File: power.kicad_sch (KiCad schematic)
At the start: 18 parts

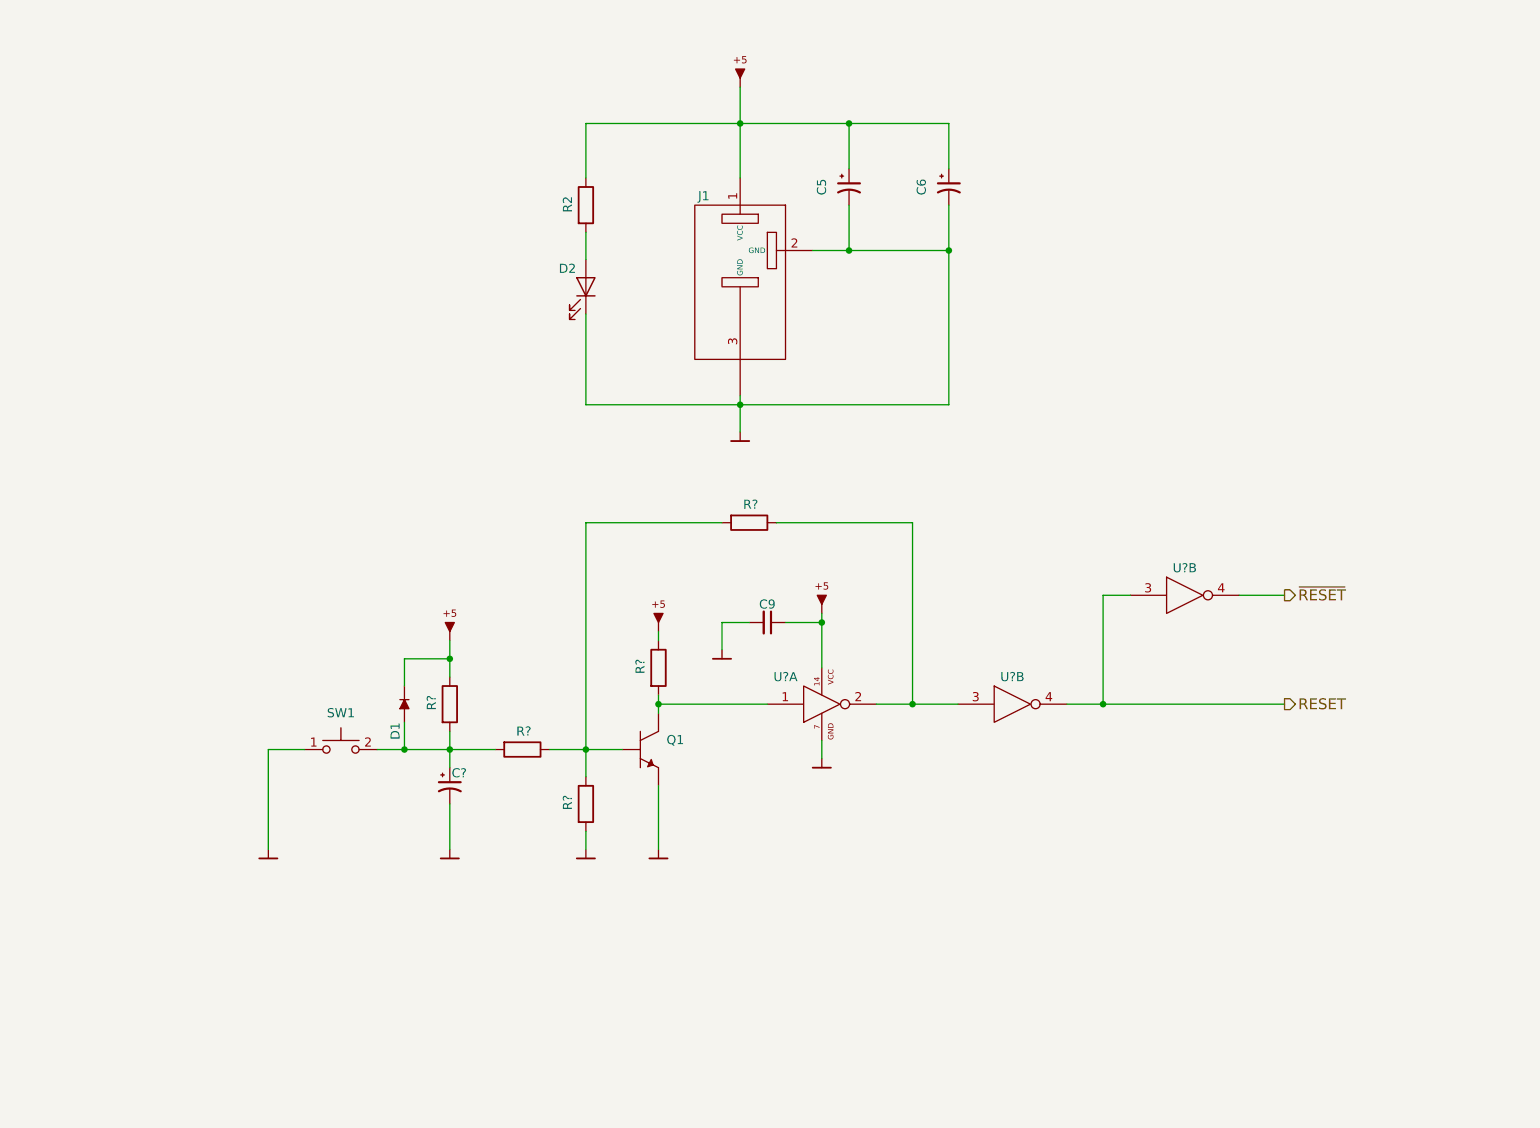
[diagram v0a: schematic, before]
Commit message: Implement power transform circuit
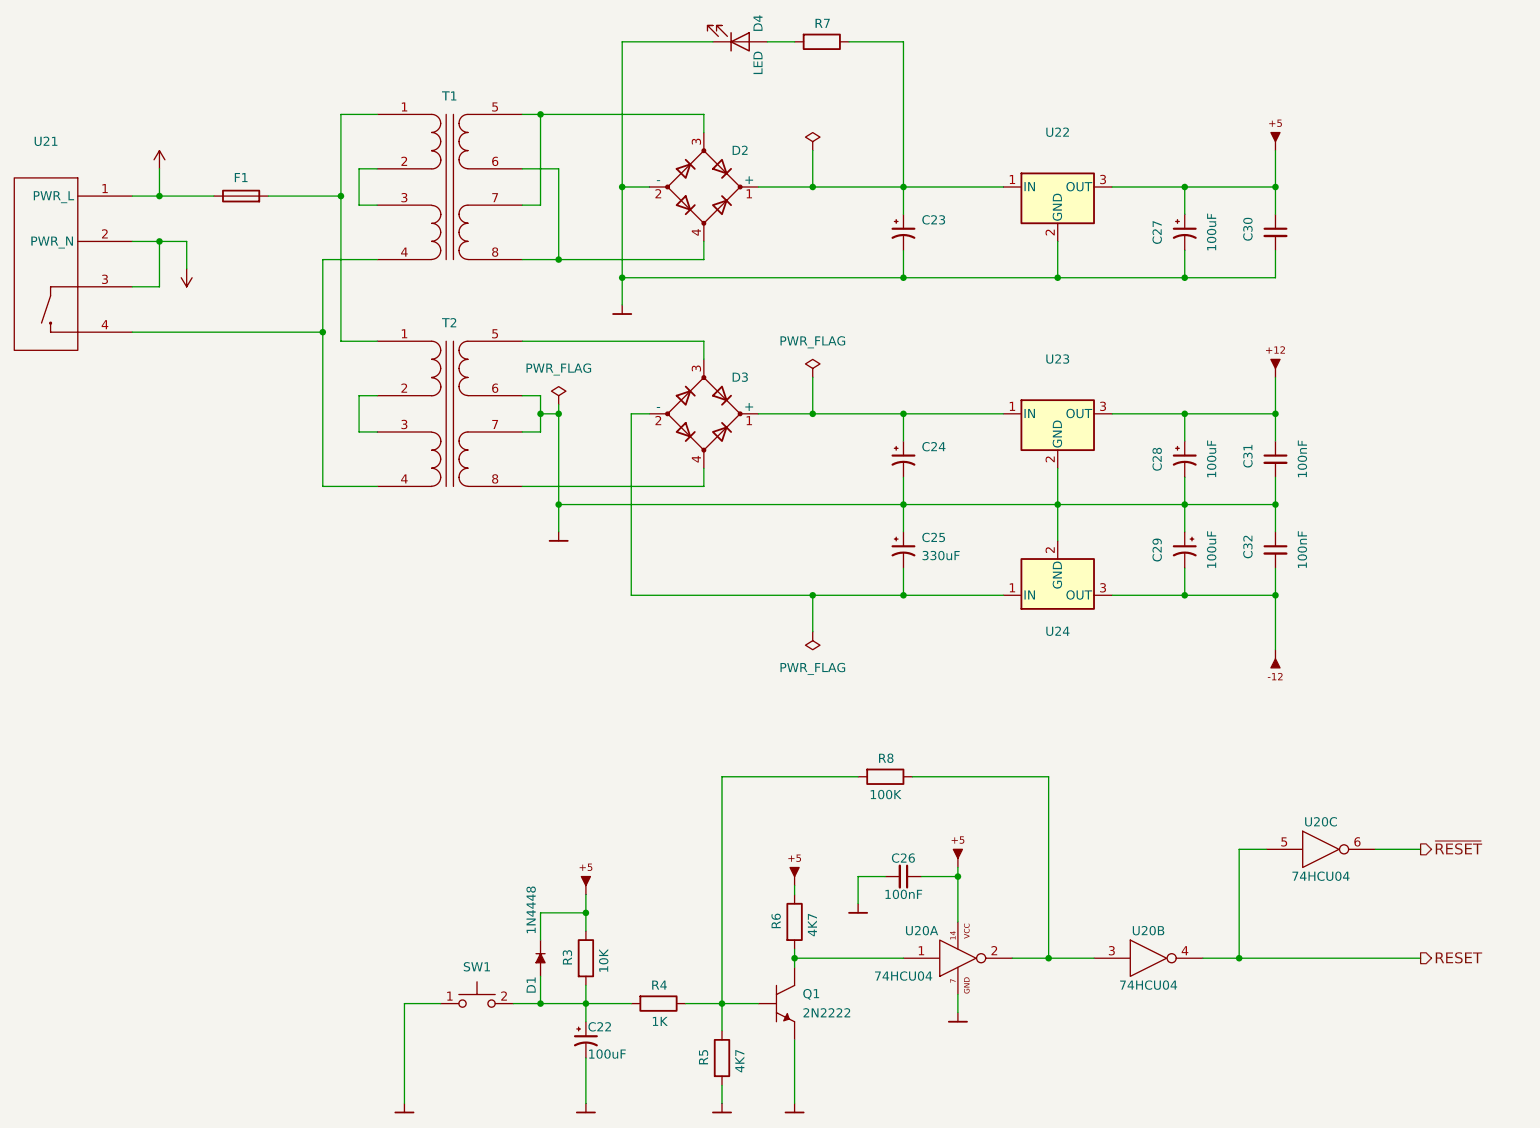
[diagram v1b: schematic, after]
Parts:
- removed C6: (no value), symbol artemisa:CP
- removed J1: (no value), symbol artemisa:PWR_conn
- added C23, C24: (no value), symbol artemisa:CP
- added C25: 330uF, symbol artemisa:CP
- added C28, C29: 100uF, artemisa:Radial_capacitor, symbol artemisa:CP
- added C30: (no value), symbol artemisa:Cap
- added C31, C32: 100nF, symbol artemisa:Cap
- added D2, D3: (no value), symbol artemisa:D_Bridge_+-AA
- added F1: (no value), symbol artemisa:Fuse
- added T1, T2: (no value), symbol artemisa:Transformer_DP_DS
- added U21: (no value), symbol artemisa:Power_conn_switched
- added U22: (no value), symbol artemisa:L7805
- added U23: (no value), symbol artemisa:L7812
- added U24: (no value), symbol artemisa:L7912
- C22: renamed from C?; value (none) -> 100uF; footprint (none) -> artemisa:Radial_capacitor
- C26: renamed from C9; value (none) -> 100nF; footprint (none) -> artemisa:Disc_capacitor
- C27: renamed from C5; value (none) -> 100uF; footprint (none) -> artemisa:Radial_capacitor
- D1: value (none) -> 1N4448; footprint (none) -> artemisa:Axial_diode
- D4: renamed from D2; value (none) -> LED; footprint (none) -> artemisa:LED
- Q1: value (none) -> 2N2222; footprint (none) -> artemisa:TO92
- R3: renamed from R?; value (none) -> 10K; footprint (none) -> artemisa:Axial_resistor
- R4: renamed from R?; value (none) -> 1K; footprint (none) -> artemisa:Axial_resistor
- R5, R6: renamed from R?; value (none) -> 4K7; footprint (none) -> artemisa:Axial_resistor
- R7: renamed from R2; footprint (none) -> artemisa:Axial_resistor
- R8: renamed from R?; value (none) -> 100K; footprint (none) -> artemisa:Axial_resistor
- SW1: value (none) -> Push_button; footprint (none) -> artemisa:Push_button_angled
- U20: renamed from U?; value (none) -> 74HCU04; footprint (none) -> artemisa:DIP-14_300
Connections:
- net GND: now also C23.2, C24.2, C25.1, C28.2, C29.1, C30.2, C31.2, C32.1, D2.2 (-), T2.6 (OUT1B), T2.7 (OUT2A), U22.2 (GND), U23.2 (GND), U24.2 (GND)
- net RESET: now also U20.5; no longer U20.3
- net ~{RESET}: now also U20.6; no longer U20.4
- net at R7.1: now also C23.1, D2.1 (+), U22.1 (IN); no longer C27.1
- net VCC: now reaches C26.1, U20.14 (VCC)
- net VCC: now also C27.1, D1.2, R3.1, R6.1, C30.1, U22.3 (OUT)
- new net: F1.2, T1.1 (IN1A), T2.1 (IN1A)
- new net: T1.2 (IN1B), T1.3 (IN2A)
- new net: T1.4 (IN2B), T2.4 (IN2B), U21.4
- new net: D2.3, T1.5 (OUT1A), T1.7 (OUT2A)
- new net: D2.4, T1.6 (OUT1B), T1.8 (OUT2B)
- new net: C24.1, D3.1 (+), U23.1 (IN)
- new net: C25.2, D3.2 (-), U24.1 (IN)
- new net: D3.3, T2.5 (OUT1A)
- new net: D3.4, T2.8 (OUT2B)
- new net: T2.2 (IN1B), T2.3 (IN2A)
- new net +12V: C28.1, C31.1, U23.3 (OUT)
- new net -12V: C29.2, C32.2, U24.3 (OUT)
- new net LINE: F1.1, U21.1 (PWR_L)
- new net NEUT: U21.2 (PWR_N), U21.3
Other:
- moved on the sheet: C22, C26, C27, D1, D4, Q1, R3, R4, R5, R6, R7, R8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
